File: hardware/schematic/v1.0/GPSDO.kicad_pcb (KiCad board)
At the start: 2 copper layers, 63 parts, among them J1 USB_C_Receptacle_USB2.0_16P, Q1 NMOS, SW1 SW_Push, U1 STM32G431KBUx, U2 OCXO-10M, U3 SKG123N, U5 BQ25890, U6 TPS7A8901, U7 CH340E, Y1 Crystal_GND24

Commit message: 更新 GPSDO 硬件原理图和 PCB 文件
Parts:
- Q1: value NMOS -> AO3400A; footprint Button_Switch_SMD:SW_SPST_B3S-1100 -> Package_TO_SOT_SMD:SOT-23-3
- moved R18 98.0 mm to (145.0, 129.3)
- moved C24 98.0 mm to (169.5, 109.6)
- moved U5 98.0 mm to (156.1, 127.2)
- moved C10 98.0 mm to (171.5, 128.6)
- moved C11 98.0 mm to (171.5, 124.1)
- moved C12 98.0 mm to (157.2, 118.1)
- moved C13 98.0 mm to (153.7, 122.1)
- moved C14 98.0 mm to (157.2, 122.1)
- moved C15 98.0 mm to (160.5, 125.1)
- moved C16 98.0 mm to (163.5, 125.1)
- moved C18 98.0 mm to (157.2, 120.1)
- moved C19 98.0 mm to (161.5, 101.6)
- moved C20 98.0 mm to (161.5, 107.6)
- moved C21 98.0 mm to (149.5, 105.3)
- moved C22 98.0 mm to (165.0, 101.6)
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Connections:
- Q1 pad 1: Net-(BZ1--) -> BUZZ
- Q1 pad 2: BUZZ -> BAT-
- Q1 pad 3: BAT- -> Net-(BZ1--)

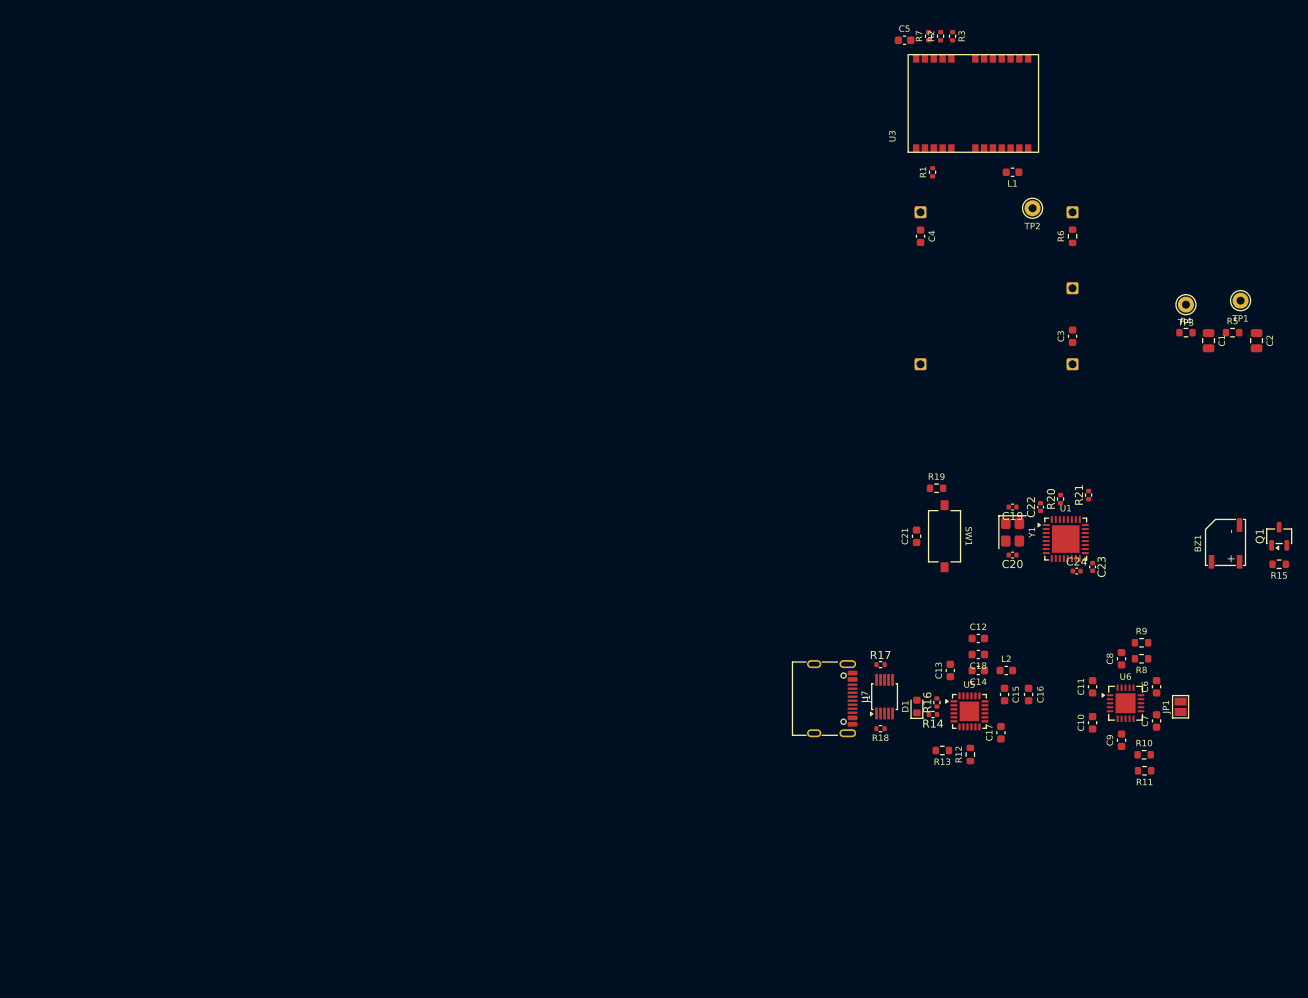
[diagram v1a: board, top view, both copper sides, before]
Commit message: 更新 GPSDO 硬件原理图和 PCB 设计文件
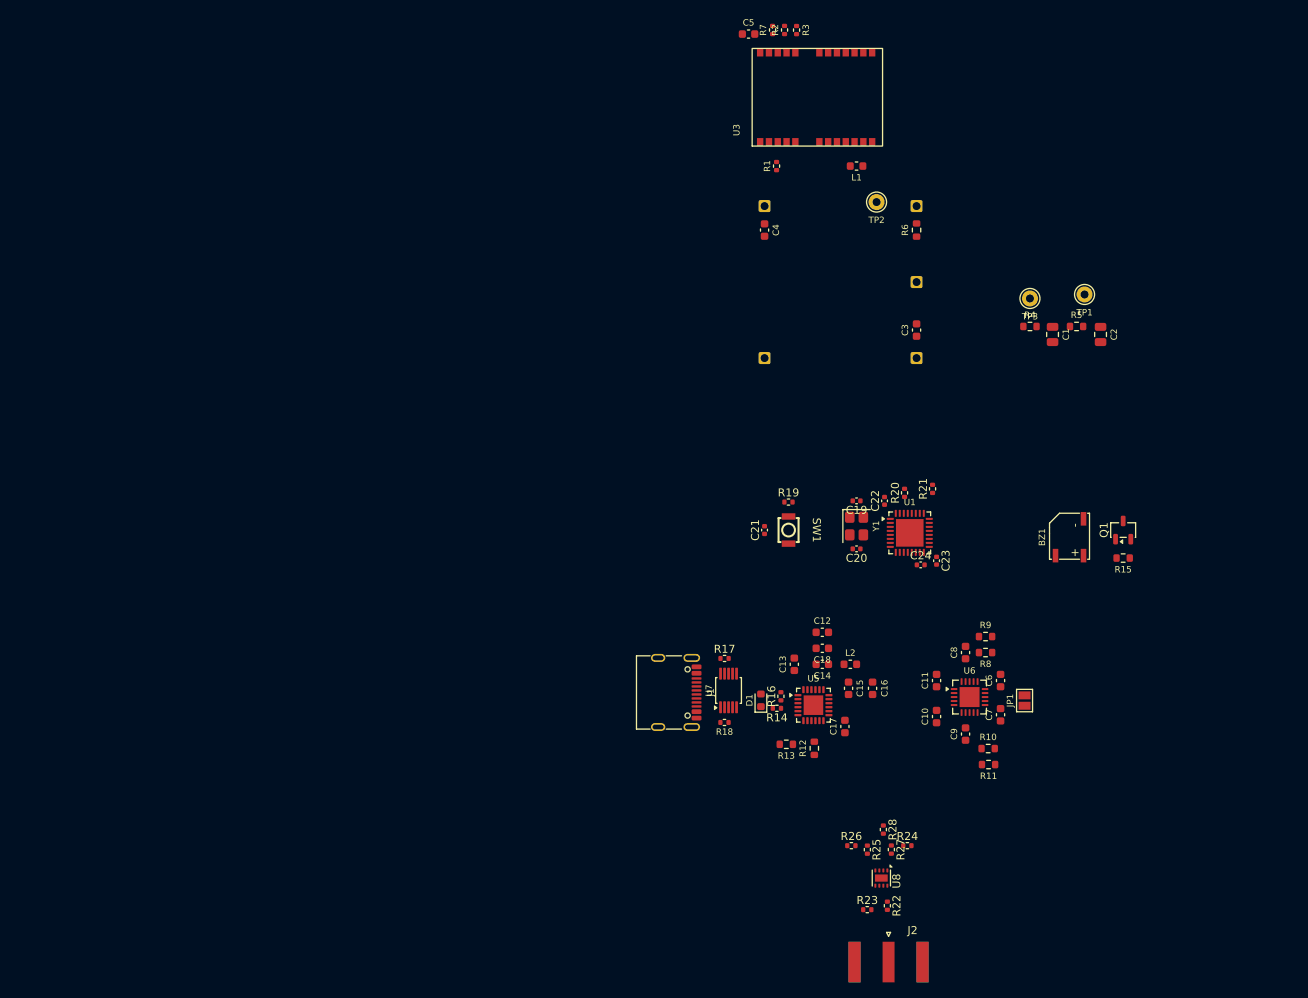
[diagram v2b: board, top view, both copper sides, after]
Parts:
- added J2: Conn_Coaxial, Connector_Coaxial:SMA_Amphenol_132289_EdgeMount, F.Cu at (146.0, 158.5)
- added R22: 0, Resistor_SMD:R_0402_1005Metric, F.Cu at (145.8, 151.5)
- added R23: 49.9 %1, Resistor_SMD:R_0402_1005Metric, F.Cu at (143.3, 151.9)
- added R24: 49.9 %1, Resistor_SMD:R_0402_1005Metric, F.Cu at (148.3, 143.9)
- added R25: 0, Resistor_SMD:R_0402_1005Metric, F.Cu at (143.3, 144.4)
- added R26: 49.9 %1, Resistor_SMD:R_0402_1005Metric, F.Cu at (141.3, 143.9)
- added R27: 0, Resistor_SMD:R_0402_1005Metric, F.Cu at (146.3, 144.4)
- added R28: 10K, Resistor_SMD:R_0402_1005Metric, F.Cu at (145.3, 141.9)
- added U8: LMK1C1102, Package_SON:WSON-8-1EP_2x2mm_P0.5mm_EP0.9x1.6mm, F.Cu at (145.1, 148.0)
- C21: footprint Capacitor_SMD:C_0603_1608Metric -> Capacitor_SMD:C_0402_1005Metric
- R19: footprint Resistor_SMD:R_0603_1608Metric -> Resistor_SMD:R_0402_1005Metric
- SW1: footprint Button_Switch_SMD:SW_Tactile_SPST_NO_Straight_CK_PTS636Sx25SMTRLFS -> Counter:KEY-SMD_B3U-1000PM
- moved R18 19.5 mm to (125.5, 128.6)
- moved BZ1 19.5 mm to (168.6, 105.4)
- moved C1 19.5 mm to (166.5, 80.0)
- moved C10 19.5 mm to (152.0, 127.8)
- moved C11 19.5 mm to (152.0, 123.3)
- moved C12 19.5 mm to (137.7, 117.3)
- moved C13 19.5 mm to (134.2, 121.3)
- moved C14 19.5 mm to (137.7, 121.3)
- moved C15 19.5 mm to (141.0, 124.3)
- moved C16 19.5 mm to (144.0, 124.3)
- moved C17 19.5 mm to (140.5, 129.1)
- moved C18 19.5 mm to (137.7, 119.3)
- moved C19 19.5 mm to (142.0, 100.8)
- moved C2 19.5 mm to (172.5, 80.0)
- moved C20 19.5 mm to (142.0, 106.8)
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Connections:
- C13 pad 1: VBUS -> VBUS/OTG
- J1 pad A4: VBUS -> VBUS/OTG
- J1 pad A9: VBUS -> VBUS/OTG
- J1 pad B4: VBUS -> VBUS/OTG
- J1 pad B9: VBUS -> VBUS/OTG
- U1 pad 5: 10MHz -> 10MHz_1
- U5 pad 1: VBUS -> VBUS/OTG

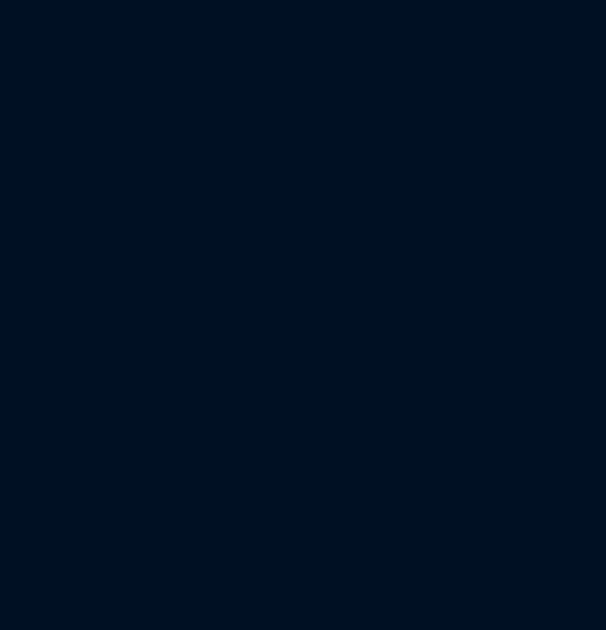
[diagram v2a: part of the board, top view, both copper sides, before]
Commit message: 更新原理图与PCB设计
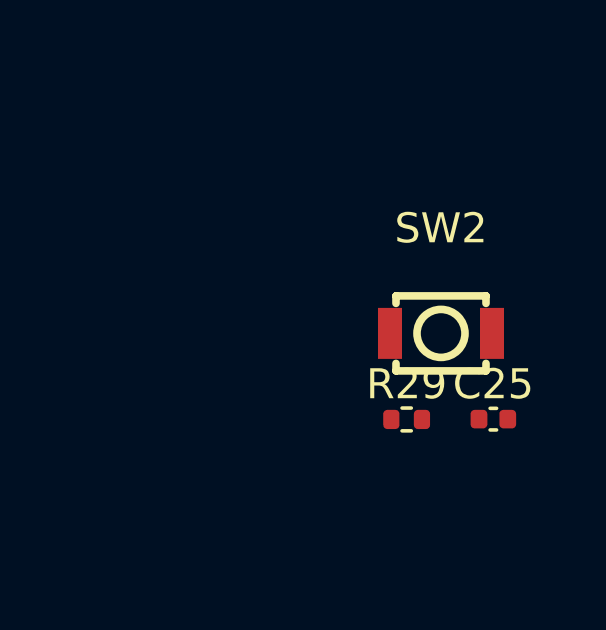
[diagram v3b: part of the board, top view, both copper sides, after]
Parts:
- added C25: 0.1uF, Capacitor_SMD:C_0402_1005Metric, F.Cu at (193.8, 125.7)
- added R29: 10K, Resistor_SMD:R_0402_1005Metric, F.Cu at (191.0, 125.7)
- added SW2: SW_Push, Counter:KEY-SMD_B3U-1000PM, F.Cu at (192.1, 122.9)
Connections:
- U5 pad 12: unconnected-(U5-QON-Pad12) -> QON

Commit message: sch update
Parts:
- added U4: IPEX1, Counter:JLC_IPEX-1, F.Cu at (148.9, 91.0)
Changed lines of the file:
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@@
+		)
+	)
+	(footprint "Counter:JLC_IPEX-1"
+		(layer "F.Cu")
+		(at 148.9 90.95)
+		(descr "-40℃~+85℃ 1 1.25mm 2mm 4GHz 50Ω Board Side IPEX Male Pin SMD Coaxial Connectors (RF) ROHS")
+		(tags "C2987682 IPEX-1 IPEX-SMD_4P-L2.6-W2.6-LS3.0 ZIISOR")
+		(property "Reference" "U4"
+			(at 0 -2.7 0)
+			(layer "F.SilkS")
+			(effects
+				(font
+					(size 1 1)
+					(thickness 0.15)
+				)
+			)
+		)
+		(property "Value" "IPEX1"
+			(at 0 2.7 0)
+			(layer "F.Fab")
+			(effects
+				(font
+					(size 1 1)
+					(thickness 0.15)
+				)
+			)
+		)
+		(property "Datasheet" ""
+			(at 0 0 0)
+			(layer "F.Fab")
+			(hide yes)
+			(effects
+				(font
+					(size 1 1)
+					(thickness 0.15)
+				)
+			)
+		)
+		(property "Description" ""
+			(at 0 0 0)
+			(layer "F.Fab")
+			(hide yes)
+			(effects
+				(font
+					(size 1 1)
+					(thickness 0.15)
+				)
+			)
+		)
+		(property "LCSC" "C2987682"
+			(at 0 0 0)
+			(layer "F.Fab")
+			(hide yes)
+			(effects
+				(font
+					(size 1 1)
+					(thickness 0.15)
+				)
+			)
+		)
+		(sheetname "/")
+		(sheetfile "GPSDO.kicad_sch")
+		(units
+			(unit
+				(name "A")
+				(pins "4" "3" "2" "1")
+			)
+		)
+		(attr smd)
+		(duplicate_pad_numbers_are_jumpers no)
+		(fp_line
+			(start -1.36 -1.36)
+			(end -0.65 -1.36)
+			(stroke
+				(width 0.1)
+				(type solid)
+			)
+			(layer "F.SilkS")
+		)
+		(fp_line
+			(start -1.36 -1.154125)
+			(end -1.36 -1.36)
+			(stroke
+				(width 0.1)
+				(type solid)
+			)
+			(layer "F.SilkS")
+		)
+		(fp_line
+			(start -1.36 1.31)
+			(end -1.36 1.154151)
+			(stroke
+				(width 0.1)
+				(type solid)
+			)
+			(layer "F.SilkS")
+		)
+		(fp_line
+			(start -0.554126 1.31)
+			(end -1.36 1.31)
+			(stroke
+				(width 0.1)
+				(type solid)
+			)
+			(layer "F.SilkS")
+		)
+		(fp_line
+			(start 0.64 -1.35)
+			(end 1.33 -1.35)
+			(stroke
+				(width 0.1)
+				(type solid)
+			)
+			(layer "F.SilkS")
+		)
+		(fp_line
+			(start 1.33 -1.35)
+			(end 1.33 -1.154125)
+			(stroke
+				(width 0.1)
+				(type solid)
+			)
+			(layer "F.SilkS")
+		)
+		(fp_line
+			(start 1.33 1.154151)
+			(end 1.33 1.31)
+			(stroke
+				(width 0.1)
+				(type solid)
+			)
+			(layer "F.SilkS")
+		)
+		(fp_line
+			(start 1.33 1.31)
+			(end 0.554126 1.31)
+			(stroke
+				(width 0.1)
+				(type solid)
+			)
+			(layer "F.SilkS")
+		)
+		(fp_circle
+			(center 0 0)
+			(end 0.2 0)
+			(stroke
+				(width 0.4)
+				(type solid)
+			)
+			(fill yes)
+			(layer "F.SilkS")
+		)
+		(fp_poly
+			(pts
+				(xy 0.18 0.66) (xy 0.18 0.342) (xy 0.17 0.332) (xy -0.16 0.332) (xy -0.16 0.67785) (xy -0.15 0.687857)
+				(xy 0.152 0.687857) (xy 0.18 0.66)
+			)
+			(stroke
+				(width 0)
+				(type solid)
+			)
+			(fill yes)
+			(layer "F.SilkS")
+		)
+		(fp_poly
+			(pts
+				(xy 0.28 0.81) (xy 0.3 0.469494) (xy 0.381 0.342494) (xy 0.508 0.088494) (xy 0.508 -0.102) (xy 0.381 -0.356)
+				(xy 0 -0.483) (xy -0.381 -0.356) (xy -0.508 0.025) (xy -0.48 0.18) (xy -0.41 0.28) (xy -0.3 0.406)
+				(xy -0.29 0.82)
+			)
+			(stroke
+				(width 0)
+				(type solid)
+			)
+			(fill yes)
+			(layer "F.Fab")
+		)
+		(pad "1" smd rect
+			(at -1.3 0 90)
+			(size 2 0.8)
+			(layers "F.Cu" "F.Mask" "F.Paste")
+			(net "BAT-")
+			(pinfunction "GND_1")
+			(pintype "input")
+		)
+		(pad "2" smd rect
+			(at 0 -1.3 180)
+			(size 0.8 0.8)
+			(layers "F.Cu" "F.Mask" "F.Paste")
+			(net "BAT-")
+			(pinfunction "GND_2")
+			(pintype "input")
+		)
+		(pad "3" smd rect
+			(at 1.3 0 90)
+			(size 2 0.8)
+			(layers "F.Cu" "F.Mask" "F.Paste")
+			(net "BAT-")
+			(pinfunction "GND_3")
+			(pintype "input")
+		)
+		(pad "4" smd rect
+			(at 0.000254 1.3 270)
+			(size 0.8 0.8)
+			(layers "F.Cu" "F.Mask" "F.Paste")
+			(net "Net-(U3-RF_IN)")
+			(pinfunction "SIG_4")
+			(pintype "input")
+		)
+		(embedded_fonts no)
+		(model "${KIPRJMOD}/JLCImport.3dshapes/IPEX-1.wrl"
+			(offset
+				(xyz 0 0 0.02)
+			)
+			(scale
+				(xyz 1 1 1)
+			)
+			(rotate
+				(xyz 0 0 0)
+			)
 		)
 	)
